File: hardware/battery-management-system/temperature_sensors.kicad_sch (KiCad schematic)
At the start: 4 parts, among them J19 TEMP_CELL1, J20 TEMP_CELL2, J21 TEMP_CELL3, J22 TEMP_CELL4

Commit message: fix design errors
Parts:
- renumbered J19 to J12, J20 to J13, J21 to J14, J22 to J15
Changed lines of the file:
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@@
   (symbol (lib_id "benediktibk:rspro_header_4pin_3_5mm") (at 58.42 53.34 0) (unit 1)
     (in_bom yes) (on_board yes) (dnp no)
-    (property "Reference" "J21" (at 60.96 53.34 0)
+    (property "Reference" "J14" (at 60.96 53.34 0)
       (effects (font (size 1.27 1.27)) (justify left))
     )
@@
       (project "battery-management-system"
         (path "/5272f0ff-3069-41a9-bca2-80beede8b4b2/3cb0d78b-1dc8-4b57-8c9a-18900dc8da61"
-          (reference "J21") (unit 1)
+          (reference "J14") (unit 1)
         )
       )
@@
   (symbol (lib_id "benediktibk:rspro_header_4pin_3_5mm") (at 58.42 27.94 0) (unit 1)
     (in_bom yes) (on_board yes) (dnp no)
-    (property "Reference" "J19" (at 60.96 27.94 0)
+    (property "Reference" "J12" (at 60.96 27.94 0)
       (effects (font (size 1.27 1.27)) (justify left))
     )
@@
       (project "battery-management-system"
         (path "/5272f0ff-3069-41a9-bca2-80beede8b4b2/3cb0d78b-1dc8-4b57-8c9a-18900dc8da61"
-          (reference "J19") (unit 1)
+          (reference "J12") (unit 1)
         )
       )
@@
   (symbol (lib_id "benediktibk:rspro_header_4pin_3_5mm") (at 58.42 40.64 0) (unit 1)
     (in_bom yes) (on_board yes) (dnp no)
-    (property "Reference" "J20" (at 60.96 40.64 0)
+    (property "Reference" "J13" (at 60.96 40.64 0)
       (effects (font (size 1.27 1.27)) (justify left))
     )
@@
       (project "battery-management-system"
         (path "/5272f0ff-3069-41a9-bca2-80beede8b4b2/3cb0d78b-1dc8-4b57-8c9a-18900dc8da61"
-          (reference "J20") (unit 1)
+          (reference "J13") (unit 1)
         )
       )
@@
   (symbol (lib_id "power:GND") (at 49.53 74.93 0) (unit 1)
     (in_bom yes) (on_board yes) (dnp no) (fields_autoplaced)
-    (property "Reference" "#PWR073" (at 49.53 81.28 0)
+    (property "Reference" "#PWR066" (at 49.53 81.28 0)
       (effects (font (size 1.27 1.27)) hide)
     )
@@
       (project "battery-management-system"
         (path "/5272f0ff-3069-41a9-bca2-80beede8b4b2/3cb0d78b-1dc8-4b57-8c9a-18900dc8da61"
-          (reference "#PWR073") (unit 1)
+          (reference "#PWR066") (unit 1)
         )
       )
@@
   (symbol (lib_id "benediktibk:rspro_header_4pin_3_5mm") (at 58.42 66.04 0) (unit 1)
     (in_bom yes) (on_board yes) (dnp no)
-    (property "Reference" "J22" (at 60.96 66.04 0)
+    (property "Reference" "J15" (at 60.96 66.04 0)
       (effects (font (size 1.27 1.27)) (justify left))
     )
@@
       (project "battery-management-system"
         (path "/5272f0ff-3069-41a9-bca2-80beede8b4b2/3cb0d78b-1dc8-4b57-8c9a-18900dc8da61"
-          (reference "J22") (unit 1)
+          (reference "J15") (unit 1)
         )
       )

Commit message: fix design errors
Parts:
- renumbered J14 to J10, J15 to J11, J12 to J8, J13 to J9
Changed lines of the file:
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@@
   (symbol (lib_id "benediktibk:rspro_header_4pin_3_5mm") (at 58.42 53.34 0) (unit 1)
     (in_bom yes) (on_board yes) (dnp no)
-    (property "Reference" "J14" (at 60.96 53.34 0)
+    (property "Reference" "J10" (at 60.96 53.34 0)
       (effects (font (size 1.27 1.27)) (justify left))
     )
@@
       (project "battery-management-system"
         (path "/5272f0ff-3069-41a9-bca2-80beede8b4b2/3cb0d78b-1dc8-4b57-8c9a-18900dc8da61"
-          (reference "J14") (unit 1)
+          (reference "J10") (unit 1)
         )
       )
@@
   (symbol (lib_id "benediktibk:rspro_header_4pin_3_5mm") (at 58.42 27.94 0) (unit 1)
     (in_bom yes) (on_board yes) (dnp no)
-    (property "Reference" "J12" (at 60.96 27.94 0)
+    (property "Reference" "J8" (at 60.96 27.94 0)
       (effects (font (size 1.27 1.27)) (justify left))
     )
@@
       (project "battery-management-system"
         (path "/5272f0ff-3069-41a9-bca2-80beede8b4b2/3cb0d78b-1dc8-4b57-8c9a-18900dc8da61"
-          (reference "J12") (unit 1)
+          (reference "J8") (unit 1)
         )
       )
@@
   (symbol (lib_id "benediktibk:rspro_header_4pin_3_5mm") (at 58.42 40.64 0) (unit 1)
     (in_bom yes) (on_board yes) (dnp no)
-    (property "Reference" "J13" (at 60.96 40.64 0)
+    (property "Reference" "J9" (at 60.96 40.64 0)
       (effects (font (size 1.27 1.27)) (justify left))
     )
@@
       (project "battery-management-system"
         (path "/5272f0ff-3069-41a9-bca2-80beede8b4b2/3cb0d78b-1dc8-4b57-8c9a-18900dc8da61"
-          (reference "J13") (unit 1)
+          (reference "J9") (unit 1)
         )
       )
@@
   (symbol (lib_id "benediktibk:rspro_header_4pin_3_5mm") (at 58.42 66.04 0) (unit 1)
     (in_bom yes) (on_board yes) (dnp no)
-    (property "Reference" "J15" (at 60.96 66.04 0)
+    (property "Reference" "J11" (at 60.96 66.04 0)
       (effects (font (size 1.27 1.27)) (justify left))
     )
@@
       (project "battery-management-system"
         (path "/5272f0ff-3069-41a9-bca2-80beede8b4b2/3cb0d78b-1dc8-4b57-8c9a-18900dc8da61"
-          (reference "J15") (unit 1)
+          (reference "J11") (unit 1)
         )
       )

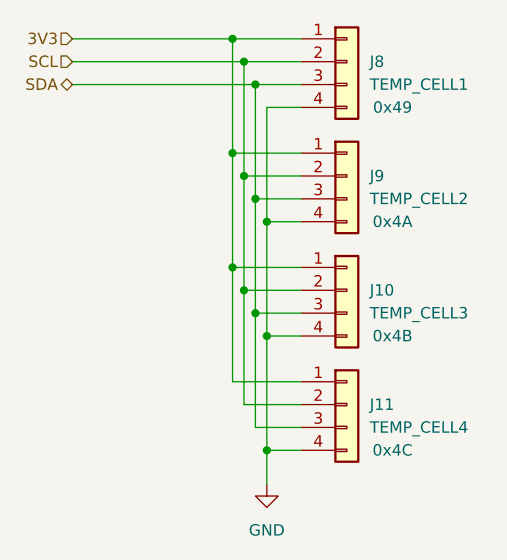
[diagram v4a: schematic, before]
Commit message: add snubber circuit
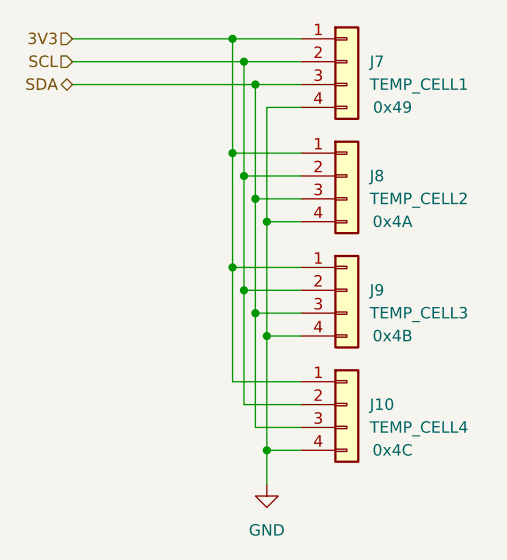
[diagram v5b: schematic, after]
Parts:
- renumbered J11 to J10, J8 to J7, J9 to J8, J10 to J9
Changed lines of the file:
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@@
 		(on_board yes)
 		(dnp no)
-		(property "Reference" "J10"
+		(property "Reference" "J9"
 			(at 60.96 53.34 0)
 			(effects
@@
 			(project "battery-management-system"
 				(path "/5272f0ff-3069-41a9-bca2-80beede8b4b2/3cb0d78b-1dc8-4b57-8c9a-18900dc8da61"
-					(reference "J10")
+					(reference "J9")
 					(unit 1)
 				)
@@
 		(on_board yes)
 		(dnp no)
-		(property "Reference" "J8"
+		(property "Reference" "J7"
 			(at 60.96 27.94 0)
 			(effects
@@
 			(project "battery-management-system"
 				(path "/5272f0ff-3069-41a9-bca2-80beede8b4b2/3cb0d78b-1dc8-4b57-8c9a-18900dc8da61"
-					(reference "J8")
+					(reference "J7")
 					(unit 1)
 				)
@@
 		(on_board yes)
 		(dnp no)
-		(property "Reference" "J9"
+		(property "Reference" "J8"
 			(at 60.96 40.64 0)
 			(effects
@@
 			(project "battery-management-system"
 				(path "/5272f0ff-3069-41a9-bca2-80beede8b4b2/3cb0d78b-1dc8-4b57-8c9a-18900dc8da61"
-					(reference "J9")
+					(reference "J8")
 					(unit 1)
 				)
@@
 		(dnp no)
 		(fields_autoplaced yes)
-		(property "Reference" "#PWR066"
+		(property "Reference" "#PWR074"
 			(at 49.53 81.28 0)
 			(effects
@@
 			(project "battery-management-system"
 				(path "/5272f0ff-3069-41a9-bca2-80beede8b4b2/3cb0d78b-1dc8-4b57-8c9a-18900dc8da61"
-					(reference "#PWR066")
+					(reference "#PWR074")
 					(unit 1)
 				)
@@
 		(on_board yes)
 		(dnp no)
-		(property "Reference" "J11"
+		(property "Reference" "J10"
 			(at 60.96 66.04 0)
 			(effects
@@
 			(project "battery-management-system"
 				(path "/5272f0ff-3069-41a9-bca2-80beede8b4b2/3cb0d78b-1dc8-4b57-8c9a-18900dc8da61"
-					(reference "J11")
+					(reference "J10")
 					(unit 1)
 				)
